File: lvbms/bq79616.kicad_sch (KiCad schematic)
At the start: 51 parts

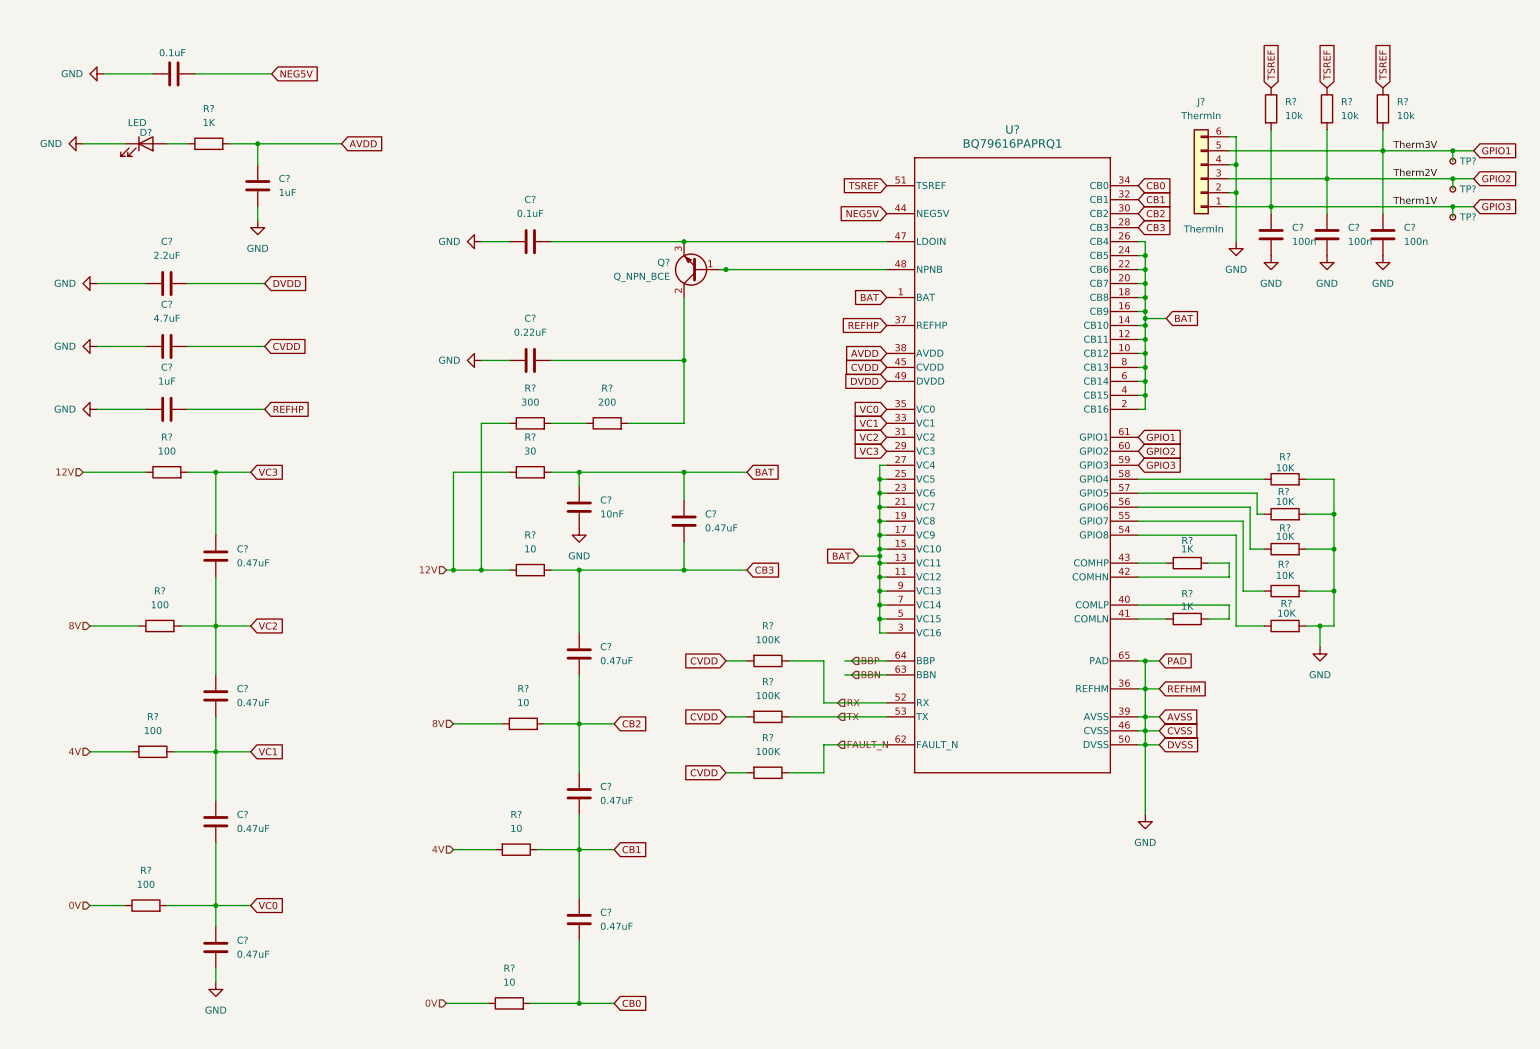
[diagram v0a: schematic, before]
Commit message: schematic seems done, component allocation next
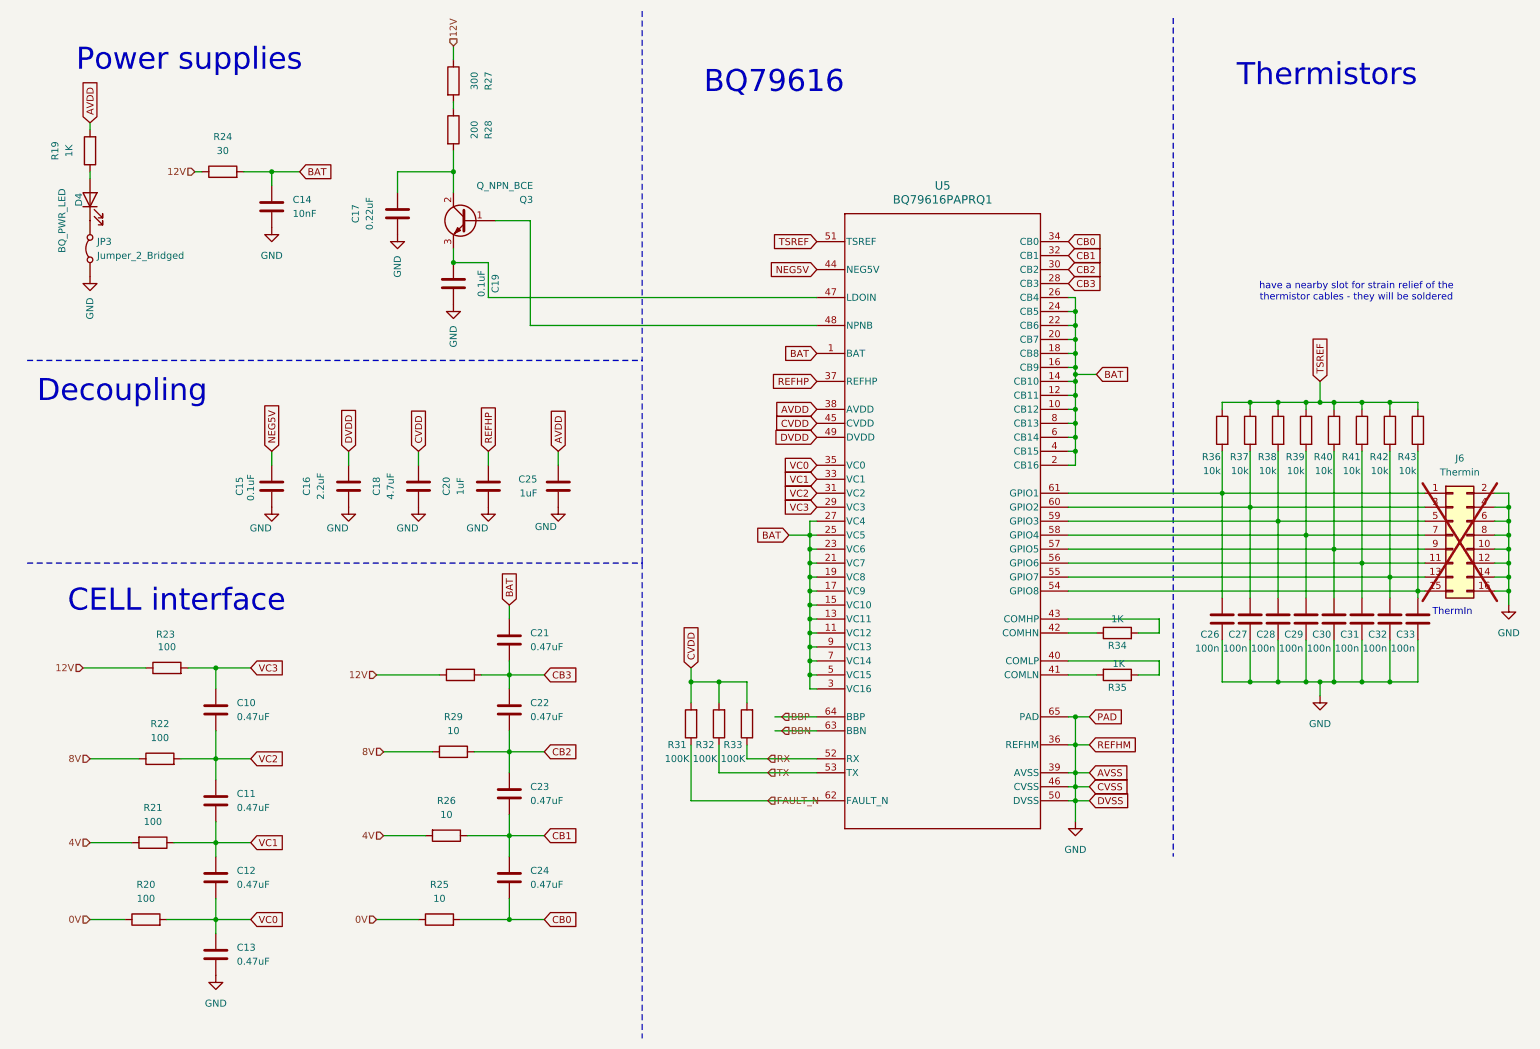
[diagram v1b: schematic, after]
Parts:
- removed C?: 1uF, symbol Device:C
- removed C?: 10nF, symbol Device:C
- removed J?: ThermIn, Connector_Molex:Molex_Micro-Fit_3.0_43650-0600_1x06_P3.00mm_Horizontal, symbol Connector_Generic:Conn_01x06
- removed R?: 30, symbol Device:R
- removed R? (x5): 10K, symbol Device:R
- removed TP? (x3): TestPoint_Small, TestPoint:TestPoint_Pad_1.5x1.5mm, symbol Connector:TestPoint_Small
- added C14: 10nF, Capacitor_SMD:C_0805_2012Metric_Pad1.18x1.45mm_HandSolder, symbol Device:C
- added C25: 1uF, Capacitor_SMD:C_0805_2012Metric_Pad1.18x1.45mm_HandSolder, symbol Device:C
- added C26, C29, C30, C32, C33: 100n, Capacitor_SMD:C_0805_2012Metric_Pad1.18x1.45mm_HandSolder, symbol Device:C
- added J6: Thermin, Connector_PinSocket_2.54mm:PinSocket_2x08_P2.54mm_Vertical, symbol Connector_Generic:Conn_02x08_Odd_Even
- added JP3: Jumper_2_Bridged, Jumper:SolderJumper-2_P1.3mm_Bridged_RoundedPad1.0x1.5mm, symbol Jumper:Jumper_2_Bridged
- added R24: 30, symbol Device:R
- added R36, R39, R40, R42, R43: 10k, Resistor_SMD:R_0805_2012Metric_Pad1.20x1.40mm_HandSolder, symbol Device:R
- C10, C11, C12, C13, C21, C22, C23, C24: renamed from C?; footprint (none) -> Capacitor_SMD:C_0805_2012Metric_Pad1.18x1.45mm_HandSolder; Order Code (none) -> 581-08055C474K4Z2A
- C15, C16, C17, C18, C19, C20: renamed from C?; footprint (none) -> Capacitor_SMD:C_0805_2012Metric_Pad1.18x1.45mm_HandSolder
- C27, C28, C31: renamed from C?; Order Code (none) -> 80-C0805C104K5RACLR; Supplier (none) -> Mouser
- D4: renamed from D?; value LED -> BQ_PWR_LED; footprint (none) -> LED_SMD:LED_0805_2012Metric_Pad1.15x1.40mm_HandSolder
- R19, R34, R35: renamed from R?; footprint (none) -> Resistor_SMD:R_0805_2012Metric_Pad1.20x1.40mm_HandSolder
- gave numbers to parts that had none: 18
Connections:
- net 12V: now also R24.1
- net AVDD: now also C25.1
- net BAT: now also C14.1, R24.2
- net GND: now also C14.2, C25.2, C26.2, C29.2, C30.2, C32.2, C33.2, J6.10 (Pin_10), J6.12 (Pin_12), J6.14 (Pin_14), J6.16 (Pin_16), J6.2 (Pin_2), J6.4 (Pin_4), J6.6 (Pin_6), J6.8 (Pin_8), JP3.1 (A); no longer D4.1 (K)
- net TSREF: now also R36.1, R39.1, R40.1, R42.1, R43.1
- net at U5.54 (GPIO8): now also C33.1, J6.15 (Pin_15), R43.2
- net at U5.55 (GPIO7): now also C32.1, J6.13 (Pin_13), R42.2
- net at U5.58 (GPIO4): now also C29.1, J6.7 (Pin_7), R39.2
- net at U5.57 (GPIO5): now also C30.1, J6.9 (Pin_9), R40.2
- net at U5.56 (GPIO6): now also C31.1, R41.2, J6.11 (Pin_11)
- net at U5.42 (COMHN): now also R34.1; no longer R34.2
- net at U5.43 (COMHP): now also R34.2; no longer R34.1
- net GPIO1: no longer names the net of C27.1, R37.2
- net GPIO1: now also U5.60 (GPIO2), J6.3 (Pin_3); no longer U5.61 (GPIO1)
- net GPIO2: no longer names the net of C28.1, R38.2
- net GPIO2: now also U5.59 (GPIO3), J6.5 (Pin_5); no longer U5.60 (GPIO2)
- removed net GPIO3: C31.1, R41.2, U5.59 (GPIO3)
- new net: C26.1, J6.1 (Pin_1), R36.2, U5.61 (GPIO1)
- new net: D4.1 (K), JP3.2 (B)
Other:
- note added: "BQ79616"
- note added: "CELL interface"
- note added: "Decoupling"
- note added: "Power supplies"
- note added: "Thermistors"
- note added: "have a nearby slot for strain relief of the thermistor cables - they will be soldered"
- moved on the sheet: C10, C11, C12, C13, C16, C17, C18, C19, C20, C21, C22, C23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

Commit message: Started V1.1 layout
BQ79616 my beloved
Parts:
- C10, C11, C12, C13, C14, C15, C16, C17, C18, C19, C20, C21, C22, C23, C24, C25, C26, C27, C28, C29, C30, C31, C32, C33: footprint Capacitor_SMD:C_0805_2012Metric_Pad1.18x1.45mm_HandSolder -> Capacitor_SMD:C_0603_1608Metric
- R19, R34, R35, R36, R37, R38, R39, R40, R41, R42, R43: footprint Resistor_SMD:R_0805_2012Metric_Pad1.20x1.40mm_HandSolder -> Resistor_SMD:R_0603_1608Metric
- R20, R21, R22, R23, R24, R27, R28, R31, R32, R33: footprint (none) -> Resistor_SMD:R_0603_1608Metric
- R25, R26, R29, R30: footprint (none) -> Resistor_SMD:R_2512_6332Metric
- U5: footprint PAP0064F-IPC_A -> sufst:PAP0064F-IPC_A

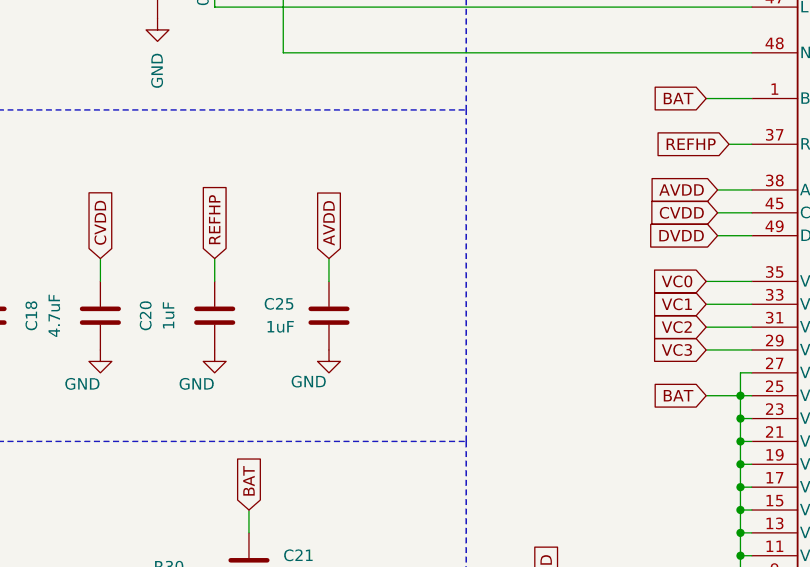
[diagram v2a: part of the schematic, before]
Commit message: DRC my beloved
don't worry about the 70 DRC errors
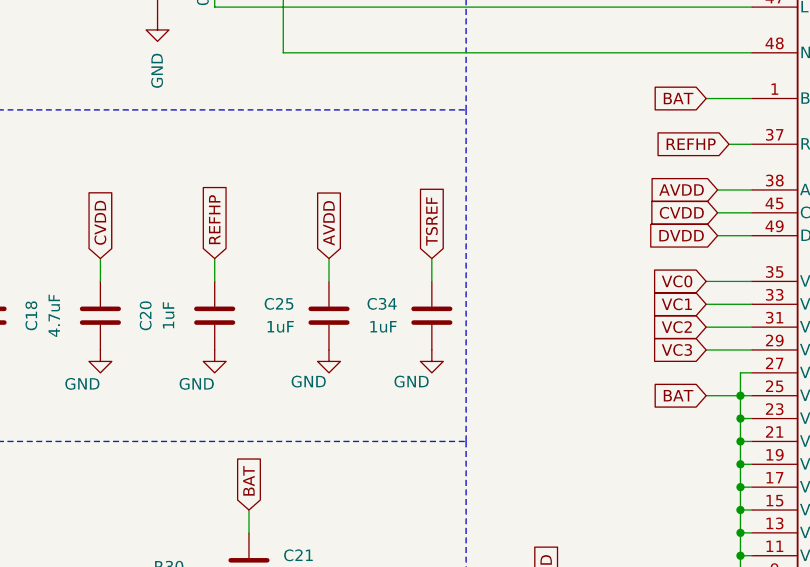
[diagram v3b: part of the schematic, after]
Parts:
- added C34: 1uF, Capacitor_SMD:C_0603_1608Metric, symbol Device:C
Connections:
- net GND: now also C34.2
- net TSREF: now also C34.1
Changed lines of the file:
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@@
 	(wire
 		(pts
+			(xy 120.65 93.98) (xy 120.65 91.44)
+		)
+		(stroke
+			(width 0)
+			(type default)
+		)
+	)
+	(wire
+		(pts
 			(xy 250.19 82.55) (xy 255.27 82.55)
 		)
@@
 		)
 	)
+	(global_label "TSREF"
+		(shape input)
+		(at 120.65 91.44 90)
+		(fields_autoplaced yes)
+		(effects
+			(font
+				(size 1.27 1.27)
+			)
+			(justify left)
+		)
+		(property "Intersheetrefs" "${INTERSHEET_REFS}"
+			(at 120.65 82.7701 90)
+			(effects
+				(font
+					(size 1.27 1.27)
+				)
+				(justify left)
+				(hide yes)
+			)
+		)
+	)
 	(global_label "VC3"
 		(shape input)
@@
 	)
 	(symbol
+		(lib_id "Device:C")
+		(at 120.65 97.79 0)
+		(mirror y)
+		(unit 1)
+		(exclude_from_sim no)
+		(in_bom yes)
+		(on_board yes)
+		(dnp no)
+		(fields_autoplaced yes)
+		(property "Reference" "C34"
+			(at 116.84 96.5199 0)
+			(effects
+				(font
+					(size 1.27 1.27)
+				)
+				(justify left)
+			)
+		)
+		(property "Value" "1uF"
+			(at 116.84 99.0599 0)
+			(effects
+				(font
+					(size 1.27 1.27)
+				)
+				(justify left)
+			)
+		)
+		(property "Footprint" "Capacitor_SMD:C_0603_1608Metric"
+			(at 119.6848 101.6 0)
+			(effects
+				(font
+					(size 1.27 1.27)
+				)
+				(hide yes)
+			)
+		)
+		(property "Datasheet" "~"
+			(at 120.65 97.79 0)
+			(effects
+				(font
+					(size 1.27 1.27)
+				)
+				(hide yes)
+			)
+		)
+		(property "Description" "Unpolarized capacitor"
+			(at 120.65 97.79 0)
+			(effects
+				(font
+					(size 1.27 1.27)
+				)
+				(hide yes)
+			)
+		)
+		(pin "2"
+		)
+		(pin "1"
+		)
+		(instances
+			(project "WholeBMS1"
+				(path "/552dda40-dad4-4f67-b96a-5b7edeb83cb9/4d2b476e-fd83-43b4-94a1-a0780a62a8e6"
+					(reference "C34")
+					(unit 1)
+				)
+			)
+		)
+	)
+	(symbol
 		(lib_id "Device:R")
 		(at 138.43 140.97 180)
@@
 					(unit 1)
 				)
+			)
+		)
+	)
+	(symbol
+		(lib_id "power:GND")
+		(at 120.65 101.6 0)
+		(mirror y)
+		(unit 1)
+		(exclude_from_sim no)
+		(in_bom yes)
+		(on_board yes)
+		(dnp no)
+		(property "Reference" "#PWR054"
+			(at 120.65 107.95 0)
+			(effects
+				(font
+					(size 1.27 1.27)
+				)
+				(hide yes)
+			)
+		)
+		(property "Value" "GND"
+			(at 120.396 105.156 0)
+			(effects
+				(font
+					(size 1.27 1.27)
+				)
+				(justify left)
+			)
+		)
+		(property "Footprint" ""
+			(at 120.65 101.6 0)
+			(effects
+				(font
+					(size 1.27 1.27)
+				)
+				(hide yes)
+			)
+		)
+		(property "Datasheet" ""
+			(at 120.65 101.6 0)
+			(effects
+				(font
+					(size 1.27 1.27)
+				)
+				(hide yes)
+			)
+		)
+		(property "Description" "Power symbol creates a global label with name \"GND\" , ground"
+			(at 120.65 101.6 0)
+			(effects
+				(font
+					(size 1.27 1.27)
+				)
+				(hide yes)
+			)
+		)
+		(pin "1"
+		)
+		(instances
+			(project "WholeBMS1"
+				(path "/552dda40-dad4-4f67-b96a-5b7edeb83cb9/4d2b476e-fd83-43b4-94a1-a0780a62a8e6"
+					(reference "#PWR054")
+					(unit 1)
+				)

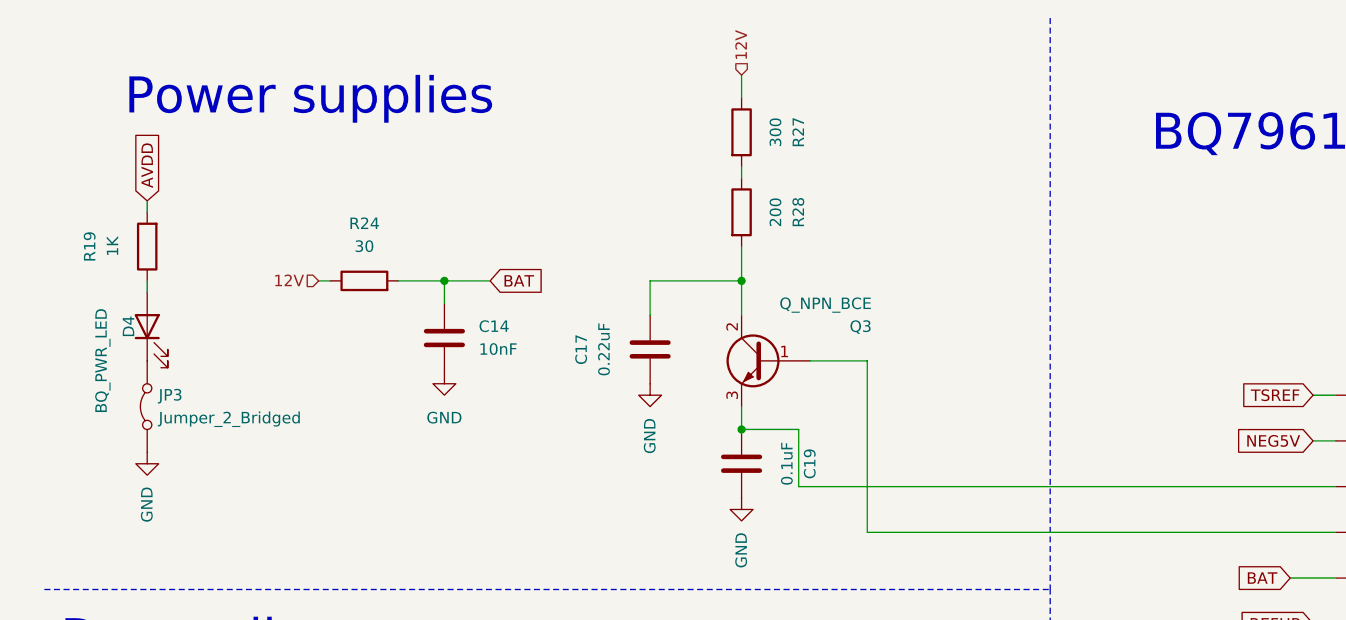
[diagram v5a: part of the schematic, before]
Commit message: the bodges needed to get it working: 	diode to prevent BQ79616 uart powering mcu 	change to 3.3v supply and change LDO to protect over current 	short relay resistor 	short bq79616 power supply resistors 	remove CAN termination 	increase shunt resistance to 4mOhm for better resolution 	open solder jumpers for leds for current consumption estimation
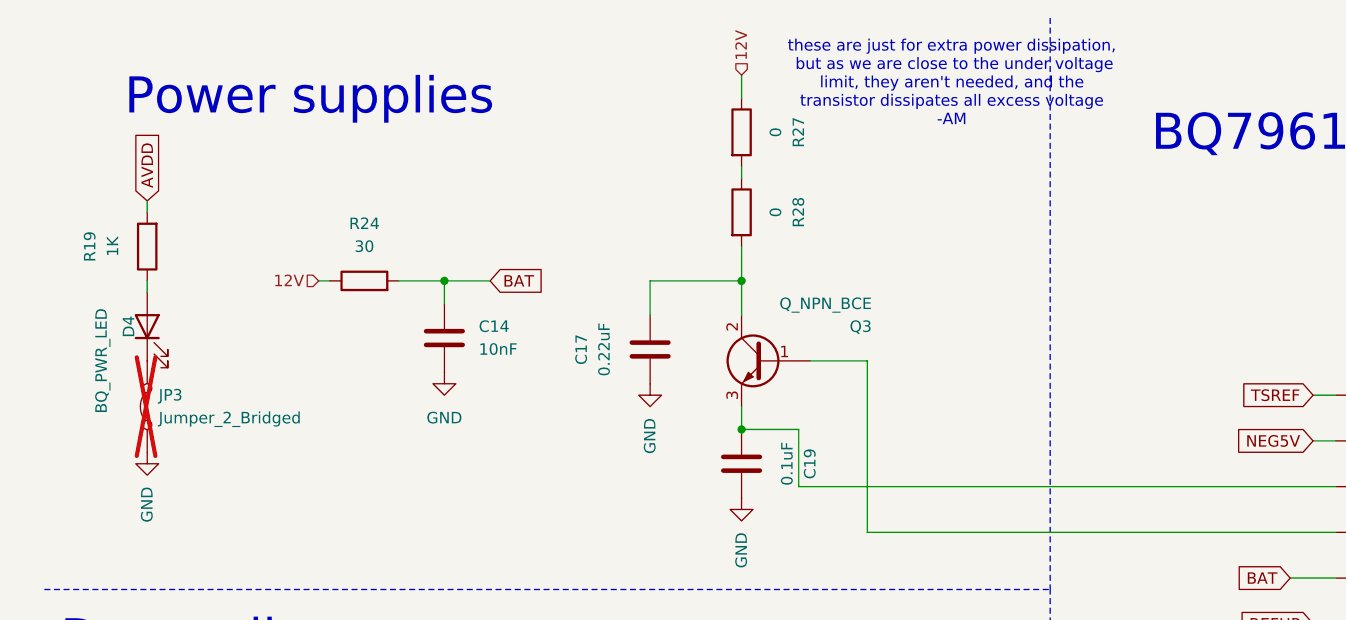
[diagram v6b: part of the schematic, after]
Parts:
- JP3: now not fitted
- R27: value 300 -> 0
- R28: value 200 -> 0
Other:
- note added: "these are just for extra power dissipation, but as we are close to the under voltage limit, they aren't needed, and the transistor dissipates all excess voltage -AM"
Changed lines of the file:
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@@
 		)
 	)
+	(text "these are just for extra power dissipation,\n but as we are close to the under voltage \nlimit, they aren't needed, and the \ntransistor dissipates all excess voltage\n-AM"
+		(exclude_from_sim no)
+		(at 113.538 18.796 0)
+		(effects
+			(font
+				(size 1.27 1.27)
+			)
+		)
+	)
 	(text "CELL interface"
 		(exclude_from_sim no)
@@
 			)
 		)
-		(property "Value" "200"
+		(property "Value" "0"
 			(at 93.98 33.02 90)
 			(effects
@@
 		(in_bom yes)
 		(on_board yes)
-		(dnp no)
+		(dnp yes)
 		(fields_autoplaced yes)
 		(property "Reference" "JP3"
@@
 			)
 		)
-		(property "Value" "300"
+		(property "Value" "0"
 			(at 93.98 24.13 90)
 			(effects
